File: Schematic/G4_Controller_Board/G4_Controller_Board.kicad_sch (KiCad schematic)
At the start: 49 parts, among them J1 Rev Trigger (Optional), J10 Solenoid, J11 Inter-board Jumper, J12 Inter-board Jumper, J13 IR LED Rec., J14 IR Led Emitter, J15 IR LED Rec., J16 IR LED Emitter, J17 Positive BUS, J18 Negative BUS, J2 ESC Right, J3 ESC Left, J4 Fire Trigger, J5 Magazine Removal Trigger, J6 Rev Trigger (Optional), J7 Fire Trigger, J8 Magazine Removal Trigger, J9 I2C Out, Q1 2N7000, Q5 Q_NMOS_GDS, Q6 Q_PMOS_GDS, SW1 Rev Switch, SW2 Preset A, SW3 Preset B, SW4 Preset C, SW5 Fire Switch, SW6 MagRemovalSwitch, SW7 RotaryEncoder_Switch, U1 ESP32-LOLIN32-Lite, U2 Mini360

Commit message: update PCB
prototype revision should be completed
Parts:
- removed D1, D2: DIODE, Diode_THT:D_DO-41_SOD81_P7.62mm_Horizontal, symbol pspice:DIODE
- added D1, D2: 1N4001, Diode_THT:D_DO-41_SOD81_P7.62mm_Horizontal, symbol Diode:1N4001
- added J12: SolenoidTrig A (Optional), Connector_PinHeader_2.54mm:PinHeader_1x03_P2.54mm_Vertical, symbol Connector_Generic:Conn_01x03
- added J13: SolenoidTrig B (Optional), Connector_PinHeader_2.54mm:PinHeader_1x03_P2.54mm_Vertical, symbol Connector_Generic:Conn_01x03
- added J21, J22: ESP32 Interconnect, Connector_PinSocket_2.54mm:PinSocket_1x13_P2.54mm_Vertical, symbol Connector_Generic:Conn_01x13
- J11: value Inter-board Jumper -> Board Interconnect; footprint Connector_PinHeader_2.54mm:PinHeader_1x09_P2.54mm_Vertical -> Connector_PinSocket_2.54mm:PinSocket_1x09_P2.54mm_Vertical
- J14: renamed from J12; value Inter-board Jumper -> Board Interconnect; footprint Connector_PinSocket_2.54mm:PinSocket_1x09_P2.54mm_Vertical -> Connector_PinHeader_2.54mm:PinHeader_1x09_P2.54mm_Vertical
- J18: renamed from J16; footprint Connector_PinSocket_2.54mm:PinSocket_1x02_P2.54mm_Vertical -> Connector_PinHeader_2.54mm:PinHeader_1x02_P2.54mm_Vertical
- J6: renamed from J9; footprint Connector_PinSocket_2.54mm:PinSocket_1x04_P2.54mm_Vertical -> Connector_PinHeader_2.54mm:PinHeader_1x04_P2.54mm_Vertical
- renumbered J13 to J15, J14 to J16, J15 to J17, J17 to J19, J18 to J20, J6 to J7, J7 to J8, J8 to J9
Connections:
- net +12V: now also D1.1 (K)
- net +3V3: now also J21.1 (Pin_1)
- net Battery Reader: now also J22.4 (Pin_4)
- net Buzzer: now also J21.13 (Pin_13)
- net ESC Left: now also J21.5 (Pin_5)
- net ESC Right: now also J21.4 (Pin_4)
- net Encoder A: now also J22.7 (Pin_7)
- net Encoder B: now also J22.8 (Pin_8)
- net Encoder Switch: now also J22.6 (Pin_6)
- net FireTrg: now also J8.1 (Pin_1), J21.6 (Pin_6); no longer J8.3 (Pin_3)
- net GND: now also J7.3 (Pin_3), J8.3 (Pin_3), J9.3 (Pin_3), D2.2 (A), J12.2 (Pin_2), J12.3 (Pin_3), J13.2 (Pin_2), J13.3 (Pin_3), J22.13 (Pin_13); no longer J7.1 (Pin_1), J8.1 (Pin_1), J9.1 (Pin_1)
- net IR Emitter: now also J21.11 (Pin_11)
- net IR Rec. Supply: now also J21.12 (Pin_12)
- net IR Reciever: now also J22.5 (Pin_5)
- net MagTrg: now also J9.1 (Pin_1), J21.7 (Pin_7); no longer J9.3 (Pin_3)
- net Preset A: now also J22.10 (Pin_10)
- net Preset B: now also J22.11 (Pin_11)
- net Preset C: now also J22.12 (Pin_12)
- net Pusher Pin: now also J22.9 (Pin_9)
- net RevTrg: now also J7.1 (Pin_1), J21.8 (Pin_8); no longer J7.3 (Pin_3)
- net SCL/SCK (Clock): now also J21.2 (Pin_2)
- net SDA/SDI (Data): now also J21.3 (Pin_3)
- net SOLENOID_A: now also D1.2 (A)
- net SOLENOID_B: now also D2.1 (K)
- net at U1.5 (VP): now also J22.1 (Pin_1)
- net at U1.8 (VN): now also J22.2 (Pin_2)
- net at U1.9 (EN): now also J22.3 (Pin_3)
- net SolenoidTrig A renamed SolTrig A
- net SolTrig A: now also J12.1 (Pin_1), J21.9 (Pin_9)
- net SolenoidTrig B renamed SolTrig B
- net SolTrig B: now also J13.1 (Pin_1), J21.10 (Pin_10)
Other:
- moved on the sheet: J11, J14, U1

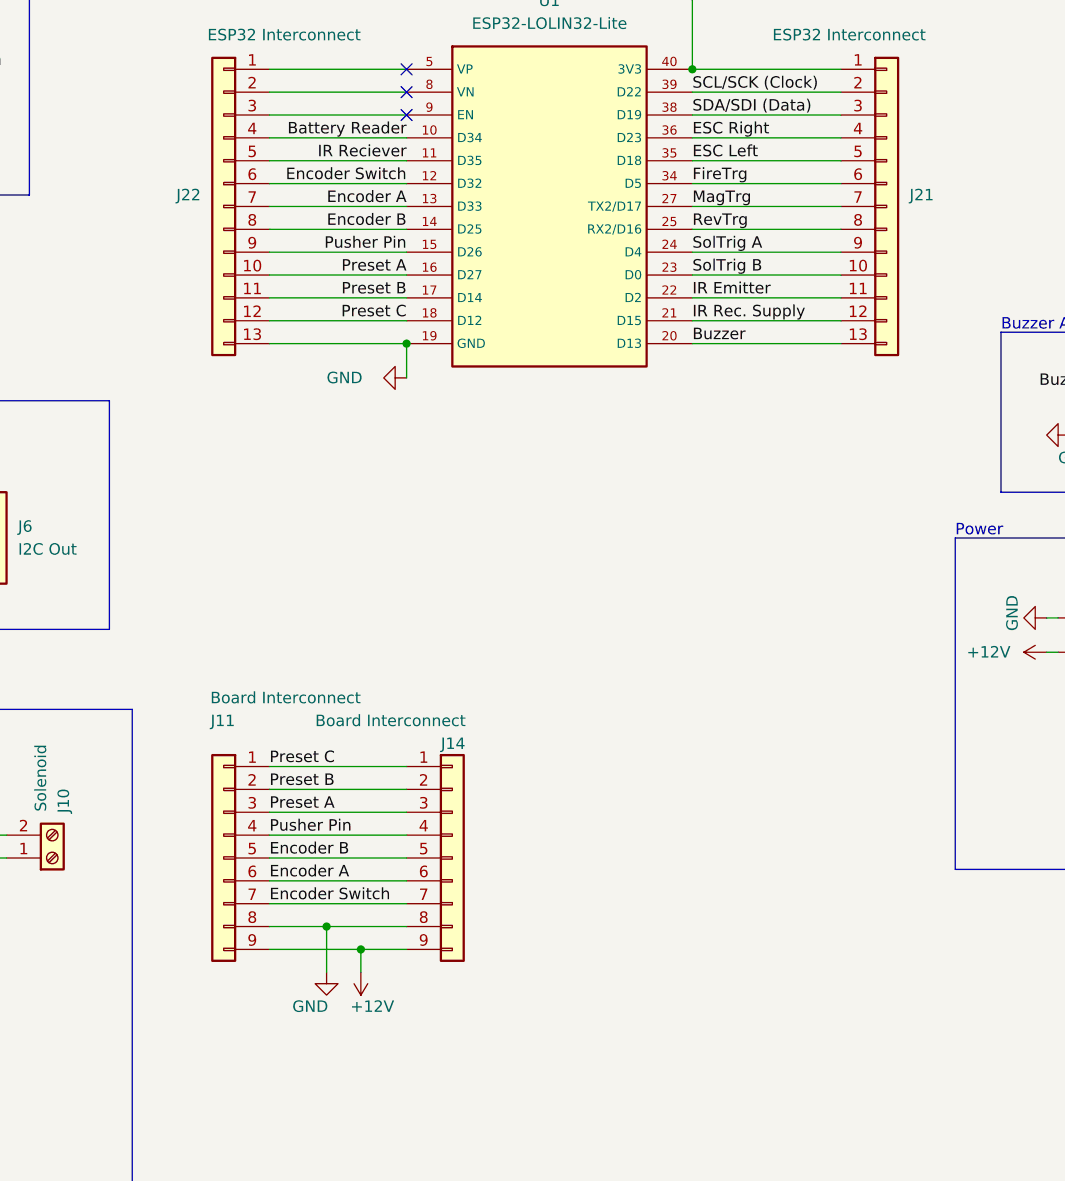
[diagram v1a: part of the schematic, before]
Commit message: update PCB
trying 3 PCB config (floating buttons, ESP32, and fast decay driver)
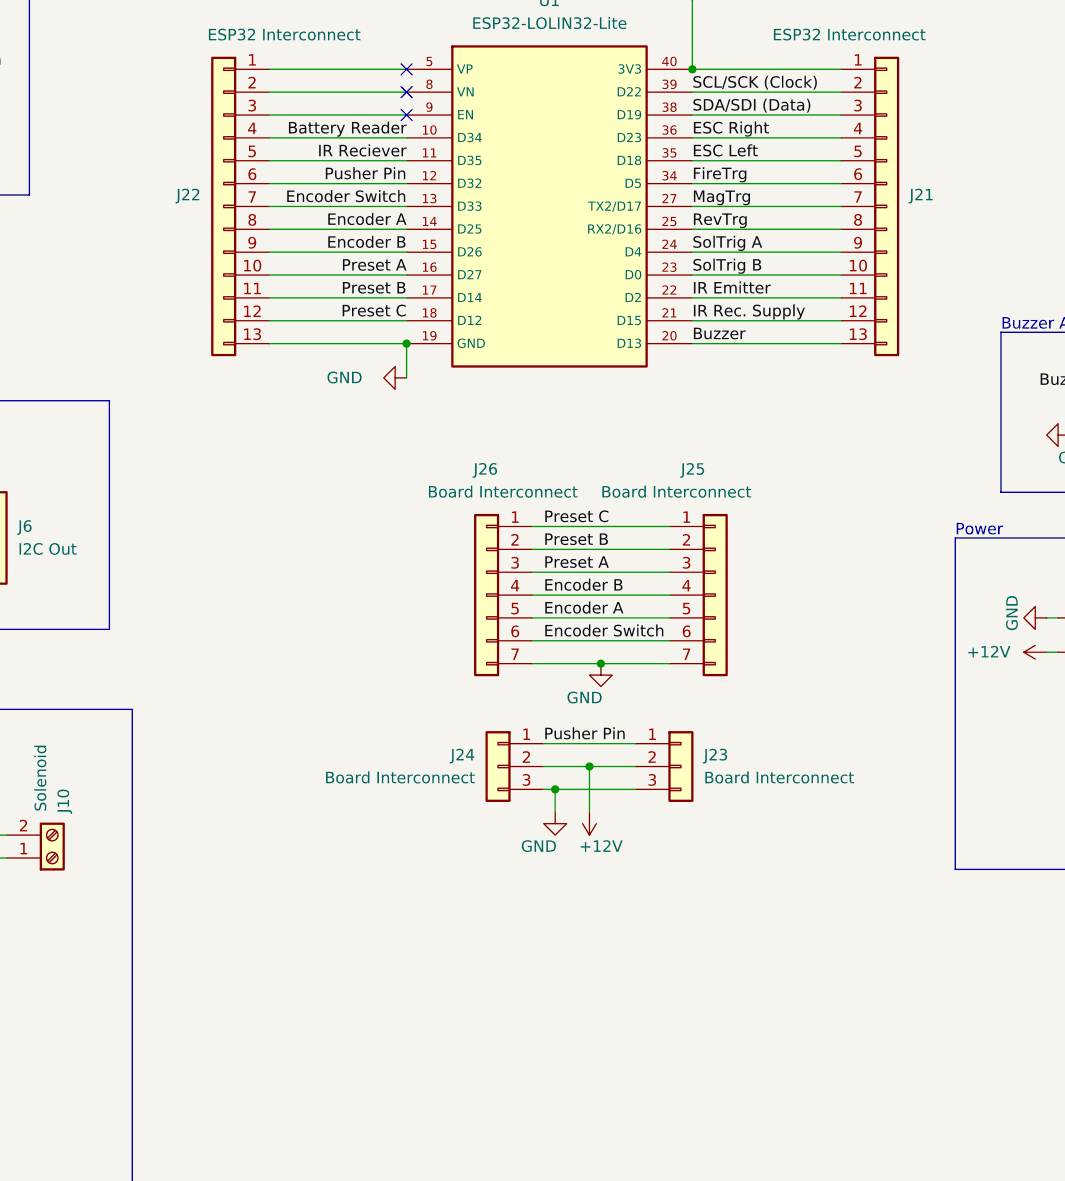
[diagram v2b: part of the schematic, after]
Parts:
- removed J11: Board Interconnect, Connector_PinSocket_2.54mm:PinSocket_1x09_P2.54mm_Vertical, symbol Connector_Generic:Conn_01x09
- removed J14: Board Interconnect, Connector_PinHeader_2.54mm:PinHeader_1x09_P2.54mm_Vertical, symbol Connector_Generic:Conn_01x09
- added J23, J24: Board Interconnect, Connector_PinHeader_2.54mm:PinHeader_1x03_P2.54mm_Vertical, symbol Connector_Generic:Conn_01x03
- added J25: Board Interconnect, Connector_PinHeader_2.54mm:PinHeader_1x07_P2.54mm_Vertical, symbol Connector_Generic:Conn_01x07
- added J26: Board Interconnect, Connector_PinHeader_2.54mm:PinHeader_1x07_P2.54mm_Horizontal, symbol Connector_Generic:Conn_01x07
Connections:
- net +12V: now also J23.2 (Pin_2), J24.2 (Pin_2)
- net Encoder A: now also J22.8 (Pin_8), U1.14 (D25), J25.5 (Pin_5), J26.5 (Pin_5); no longer J22.7 (Pin_7), U1.13 (D33)
- net Encoder B: now also J22.9 (Pin_9), U1.15 (D26), J25.4 (Pin_4), J26.4 (Pin_4); no longer J22.8 (Pin_8), U1.14 (D25)
- net Encoder Switch: now also J22.7 (Pin_7), U1.13 (D33), J25.6 (Pin_6), J26.6 (Pin_6); no longer J22.6 (Pin_6), U1.12 (D32)
- net GND: now also J23.3 (Pin_3), J24.3 (Pin_3), J25.7 (Pin_7), J26.7 (Pin_7)
- net Preset A: now also J25.3 (Pin_3), J26.3 (Pin_3)
- net Preset B: now also J25.2 (Pin_2), J26.2 (Pin_2)
- net Preset C: now also J25.1 (Pin_1), J26.1 (Pin_1)
- net Pusher Pin: now also J22.6 (Pin_6), U1.12 (D32), J23.1 (Pin_1), J24.1 (Pin_1); no longer J22.9 (Pin_9), U1.15 (D26)

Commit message: update PCB traces
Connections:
- net Encoder A: now also J22.7 (Pin_7), J25.6 (Pin_6), J26.6 (Pin_6), U1.13 (D33); no longer J22.8 (Pin_8), J25.5 (Pin_5), J26.5 (Pin_5), U1.14 (D25)
- net Encoder B: now also J22.8 (Pin_8), J25.5 (Pin_5), J26.5 (Pin_5), U1.14 (D25); no longer J22.9 (Pin_9), J25.4 (Pin_4), J26.4 (Pin_4), U1.15 (D26)
- net Encoder Switch: now also J22.12 (Pin_12), J25.1 (Pin_1), J26.1 (Pin_1), U1.18 (D12); no longer J22.7 (Pin_7), J25.6 (Pin_6), J26.6 (Pin_6), U1.13 (D33)
- net GND: now also SW2.1; no longer SW2.2
- net Preset A: now also SW2.2; no longer SW2.1
- net Preset B: now also J22.9 (Pin_9), U1.15 (D26); no longer J22.11 (Pin_11), U1.17 (D14)
- net Preset C: now also J22.11 (Pin_11), J25.4 (Pin_4), J26.4 (Pin_4), U1.17 (D14); no longer J22.12 (Pin_12), J25.1 (Pin_1), J26.1 (Pin_1), U1.18 (D12)

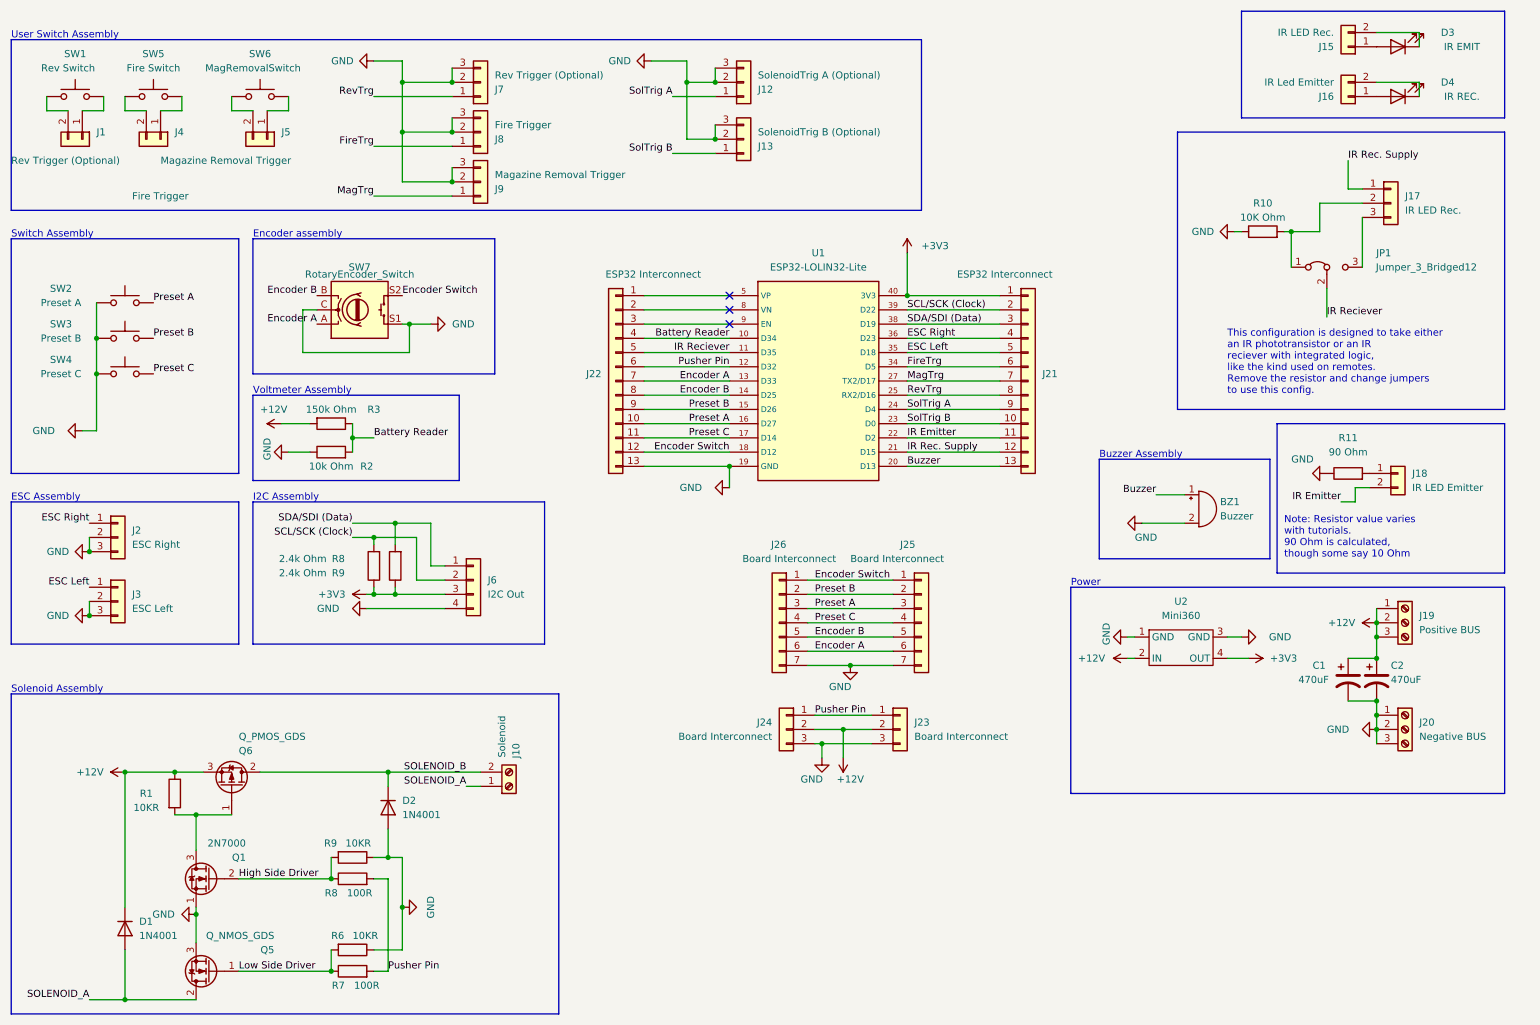
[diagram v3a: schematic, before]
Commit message: create machine code for PCB
nc code generated to machine out the physical PCB tests
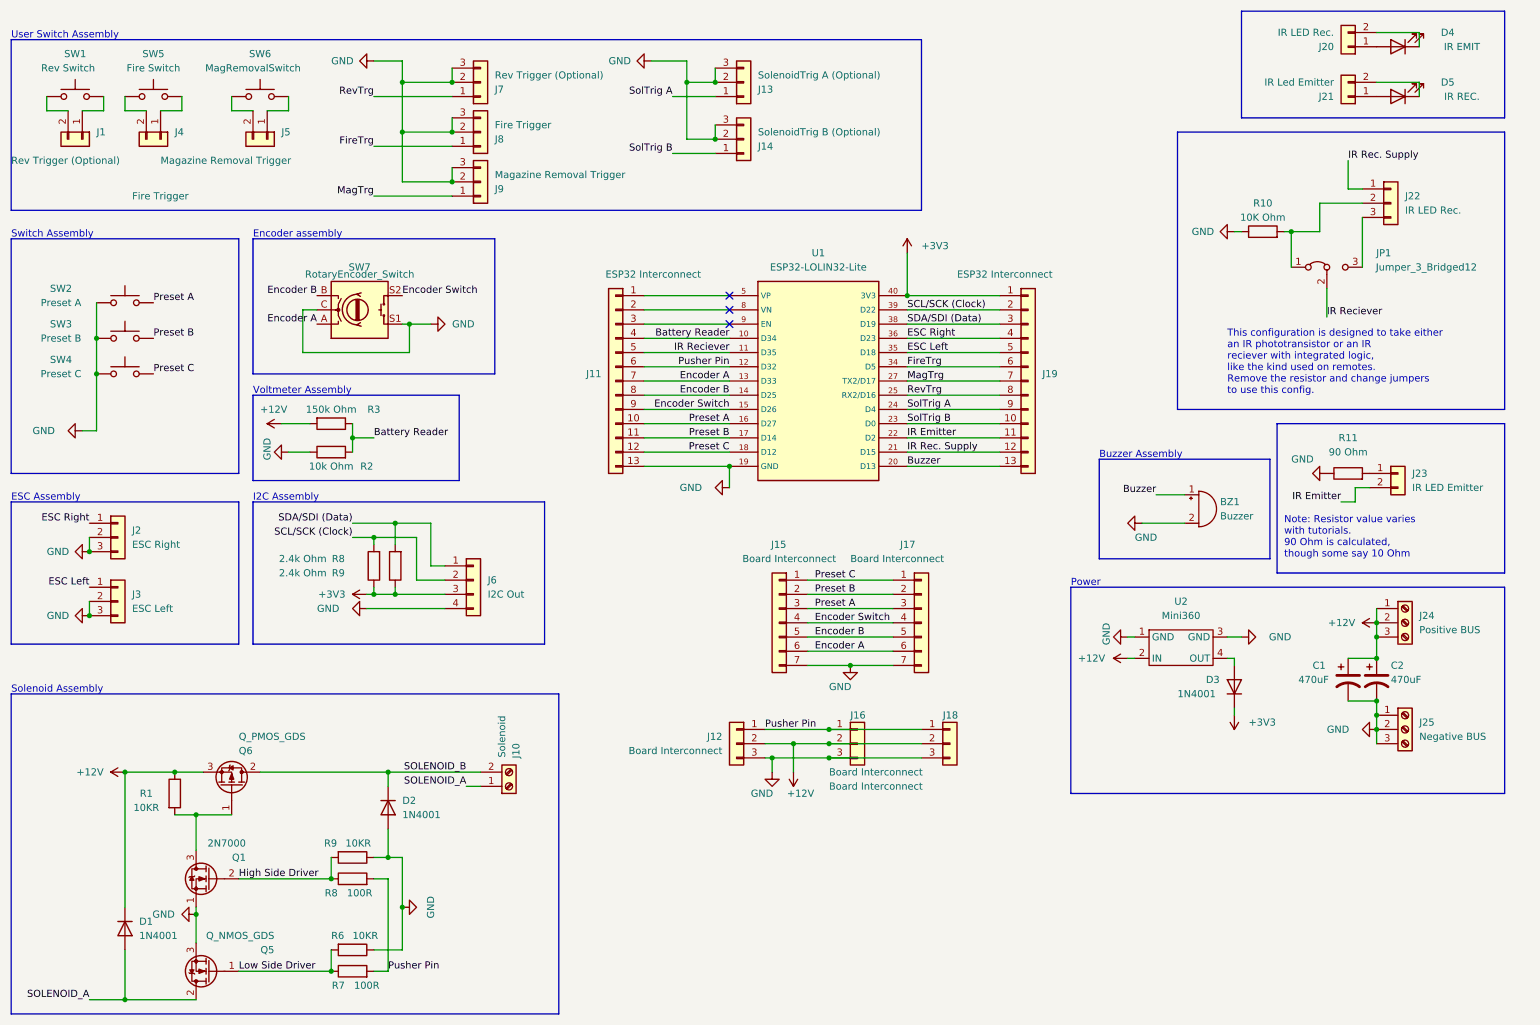
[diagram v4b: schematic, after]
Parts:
- added D3: 1N4001, Diode_THT:D_DO-41_SOD81_P7.62mm_Horizontal, symbol Diode:1N4001
- added J16: Board Interconnect, Connector_PinHeader_2.54mm:PinHeader_1x03_P2.54mm_Vertical, symbol Connector_Generic:Conn_01x03
- J18: renamed from J23; footprint Connector_PinHeader_2.54mm:PinHeader_1x03_P2.54mm_Vertical -> Connector_PinSocket_2.54mm:PinSocket_1x03_P2.54mm_Vertical
- renumbered D3 to D4, D4 to D5, J22 to J11, J24 to J12, J12 to J13, J13 to J14, J26 to J15, J25 to J17, J21 to J19, J15 to J20, J16 to J21, J17 to J22, J18 to J23, J19 to J24, J20 to J25
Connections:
- net +12V: now also J16.2 (Pin_2)
- net +3V3: now also D3.1 (K); no longer U2.4 (OUT)
- net Encoder Switch: now also J11.9 (Pin_9), J15.4 (Pin_4), J17.4 (Pin_4), U1.15 (D26); no longer J11.12 (Pin_12), J15.1 (Pin_1), J17.1 (Pin_1), U1.18 (D12)
- net GND: now also J16.3 (Pin_3)
- net Preset B: now also J11.11 (Pin_11), U1.17 (D14); no longer J11.9 (Pin_9), U1.15 (D26)
- net Preset C: now also J11.12 (Pin_12), J15.1 (Pin_1), J17.1 (Pin_1), U1.18 (D12); no longer J11.11 (Pin_11), J15.4 (Pin_4), J17.4 (Pin_4), U1.17 (D14)
- net Pusher Pin: now also J16.1 (Pin_1)
- new net: D3.2 (A), U2.4 (OUT)
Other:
- moved on the sheet: J12, J18
